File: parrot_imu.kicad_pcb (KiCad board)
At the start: 2 copper layers, 50 x 100 mm, 29 parts, among them J1 Conn_01x02_Male, J2 SI-60062-F, J3 TB005-762-02BE, U1 TR05S3V3, U2 VR10S05, U3 Spark_fun_ICM-20948, U4 Teensy4.1, U5 TJA1441AT/0Z, U6 SOT_24-2BLY_STM

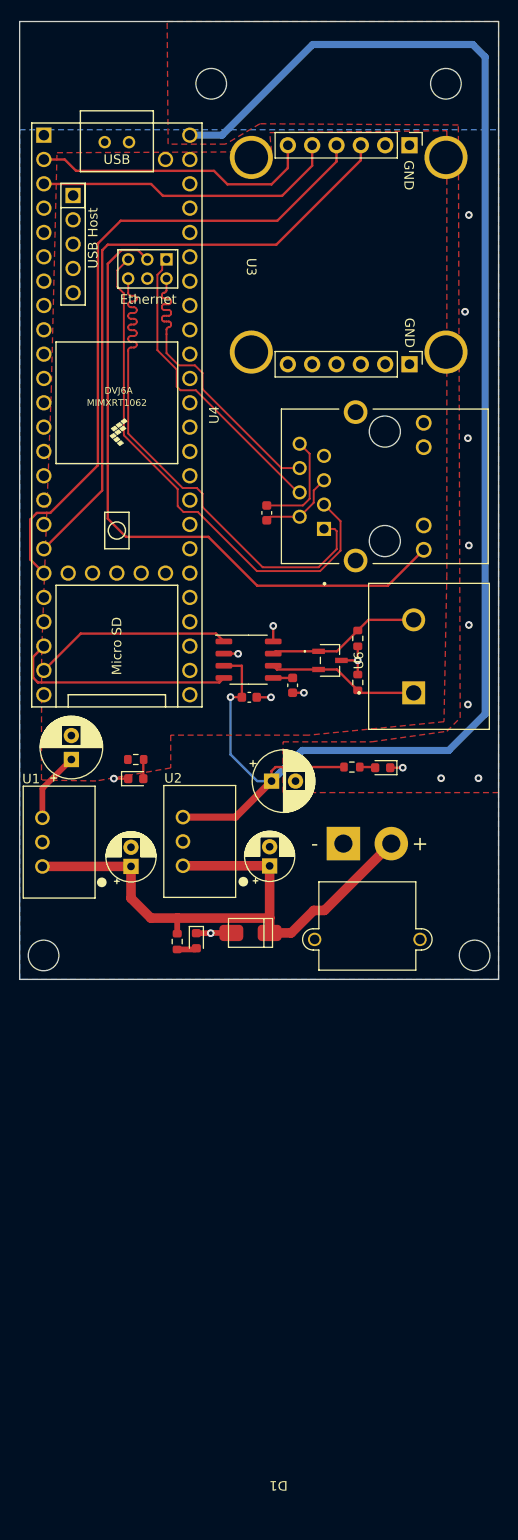
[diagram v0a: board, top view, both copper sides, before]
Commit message: silk screen stuff
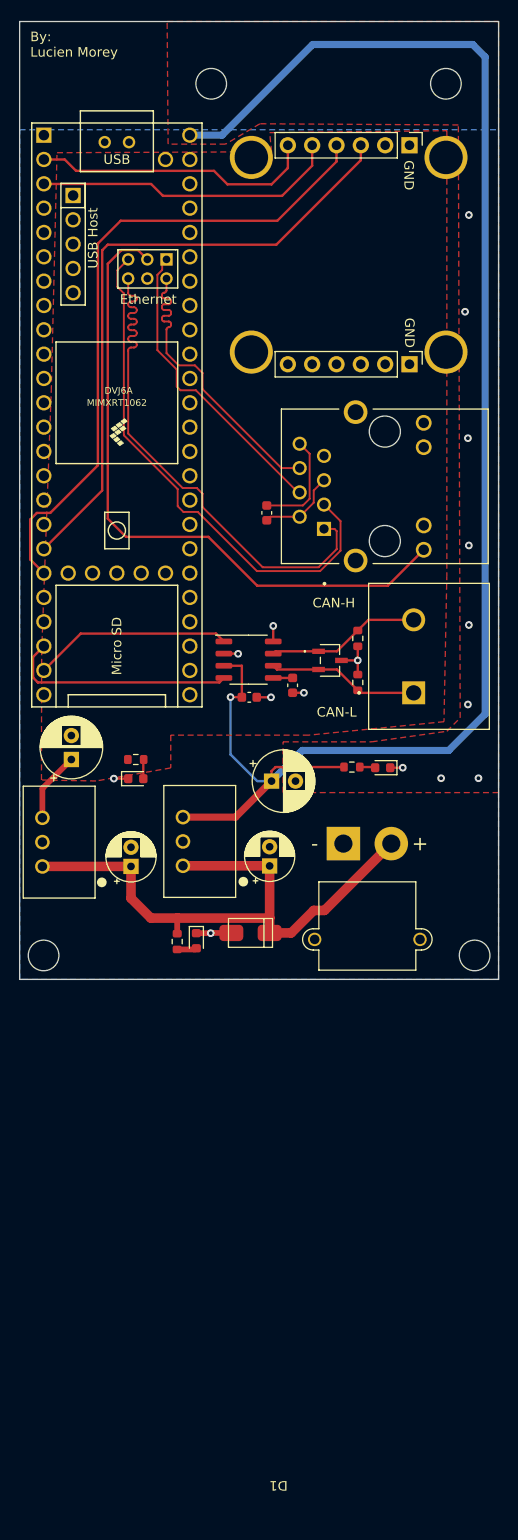
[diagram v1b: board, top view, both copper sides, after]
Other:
- board text added: "By: Lucien Morey"
- board text added: "CAN-H"
- board text added: "CAN-L"
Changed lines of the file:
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@@
     (property "Sheetname" "")
     (attr smd)
-    (fp_text reference "U3" (at -10.16 11.43 -90 unlocked) (layer "F.SilkS")
+    (fp_text reference "U3" (at -10.16 11.43 -90 unlocked) (layer "F.SilkS") hide
       (effects (font (size 1 1) (thickness 0.15)))
     )
@@
     (property "Sheetname" "")
     (attr through_hole)
-    (fp_text reference "U2" (at 6.6 -1.026393 unlocked) (layer "F.SilkS")
+    (fp_text reference "U2" (at 6.6 -1.026393 unlocked) (layer "F.SilkS") hide
       (effects (font (size 1 1) (thickness 0.15)))
     )
@@
     (property "Sheetname" "")
     (attr smd)
-    (fp_text reference "U6" (at 0 -3 -90) (layer "F.SilkS")
+    (fp_text reference "U6" (at 0 -3 -90) (layer "F.SilkS") hide
       (effects (font (size 1 1) (thickness 0.15)))
     )
@@
     (property "Sheetname" "")
     (attr through_hole)
-    (fp_text reference "U4" (at 0 -10.16 90) (layer "F.SilkS")
+    (fp_text reference "U4" (at 0 -10.16 90) (layer "F.SilkS") hide
       (effects (font (size 1 1) (thickness 0.15)))
     )
@@
     (property "Sheetname" "")
     (attr through_hole)
-    (fp_text reference "U1" (at 6.6 -1.176393 unlocked) (layer "F.SilkS")
+    (fp_text reference "U1" (at 6.6 -1.176393 unlocked) (layer "F.SilkS") hide
       (effects (font (size 1 1) (thickness 0.15)))
     )
@@
   (gr_line (start 50 49) (end 100 49) (layer "Edge.Cuts") (width 0.1))
   (gr_line (start 50 149) (end 50 49) (layer "Edge.Cuts") (width 0.1))
+  (gr_text "By:\nLucien Morey" (at 51.1 51.4) (layer "F.SilkS")
+    (effects (font (size 1 1) (thickness 0.15)) (justify left))
+  )
+  (gr_text "CAN-H" (at 82.8 109.7) (layer "F.SilkS")
+    (effects (font (size 1 1) (thickness 0.15)))
+  )
+  (gr_text "CAN-L" (at 83.1 121.1) (layer "F.SilkS")
+    (effects (font (size 1 1) (thickness 0.15)))
+  )
   (segment (start 81.825 141.8) (end 88.8 134.825) (width 1) (layer "F.Cu") (net 1))
   (segment (start 61.625 140.525) (end 63.7 142.6) (width 1) (layer "F.Cu") (net 1))
@@
   (segment (start 79.235 93.08) (end 80.274 94.119) (width 0.2) (layer "F.Cu") (net 2))
   (segment (start 76.475 113.72) (end 76.475 112.1) (width 0.25) (layer "F.Cu") (net 2))
-  (segment (start 79.375 119.075) (end 79.38 119.08) (width 0.25) (layer "F.Cu") (net 2))
   (segment (start 76.24 119.55) (end 74.75 119.55) (width 0.25) (layer "F.Cu") (net 2))
   (segment (start 72.81 115.01) (end 72.79 114.99) (width 0.25) (layer "F.Cu") (net 2))
@@
   (segment (start 76.715625 126.834375) (end 83.8625 126.834375) (width 0.25) (layer "F.Cu") (net 3))
   (segment (start 73.2 119.55) (end 73.2 116.26) (width 0.25) (layer "F.Cu") (net 3))
-  (segment (start 83.8625 126.834375) (end 83.8375 126.859375) (width 0.25) (layer "F.Cu") (net 3))
   (segment (start 72.02 119.53) (end 73.18 119.53) (width 0.25) (layer "F.Cu") (net 3))
   (segment (start 67.051393 132.06) (end 72.54 132.06) (width 0.75) (layer "F.Cu") (net 3))
@@
   (segment (start 62.9125 126.082387) (end 62.95 126.044887) (width 0.25) (layer "F.Cu") (net 6))
   (segment (start 62.9125 128.044887) (end 62.9125 126.082387) (width 0.25) (layer "F.Cu") (net 6))
-  (segment (start 85.5 126.846875) (end 85.5125 126.834375) (width 0.25) (layer "F.Cu") (net 7))
   (segment (start 87.046875 126.834375) (end 87.1125 126.9) (width 0.25) (layer "F.Cu") (net 7))
   (segment (start 85.5125 126.834375) (end 87.046875 126.834375) (width 0.25) (layer "F.Cu") (net 7))
@@
   (segment (start 64.3816 83.3066) (end 66.4 85.325) (width 0.2) (layer "F.Cu") (net 10))
   (segment (start 64.858418 79.954991) (end 64.858418 80.081809) (width 0.2) (layer "F.Cu") (net 11))
-  (segment (start 65.095009 79.1184) (end 65.3316 79.1184) (width 0.2) (layer "F.Cu") (net 11))
+  (segment (start 65.095009 79.1184) (end 65.568191 79.1184) (width 0.2) (layer "F.Cu") (net 11))
   (segment (start 69.1 87.388603) (end 77.331397 95.62) (width 0.2) (layer "F.Cu") (net 11))
-  (segment (start 65.3316 79.7184) (end 65.095009 79.7184) (width 0.2) (layer "F.Cu") (net 11))
-  (segment (start 65.3316 79.1184) (end 65.568191 79.1184) (width 0.2) (layer "F.Cu") (net 11))
+  (segment (start 65.095009 79.7184) (end 65.568191 79.7184) (width 0.2) (layer "F.Cu") (net 11))
   (segment (start 65.3316 77.904991) (end 65.3316 77.9184) (width 0.2) (layer "F.Cu") (net 11))
   (segment (start 68.3 84.9) (end 69.1 85.7) (width 0.2) (layer "F.Cu") (net 11))
   (segment (start 65.3316 83.620203) (end 66.611397 84.9) (width 0.2) (layer "F.Cu") (net 11))
-  (segment (start 65.568191 78.5184) (end 65.3316 78.5184) (width 0.2) (layer "F.Cu") (net 11))
+  (segment (start 65.095009 78.5184) (end 65.568191 78.5184) (width 0.2) (layer "F.Cu") (net 11))
   (segment (start 65.3316 75.835) (end 65.3316 77.0684) (width 0.2) (layer "F.Cu") (net 11))
-  (segment (start 65.3316 78.5184) (end 65.095009 78.5184) (width 0.2) (layer "F.Cu") (net 11))
   (segment (start 64.858418 77.541582) (end 64.858418 77.6684) (width 0.2) (layer "F.Cu") (net 11))
   (segment (start 77.331397 95.62) (end 79.235 95.62) (width 0.2) (layer "F.Cu") (net 11))
@@
   (segment (start 66.611397 84.9) (end 68.3 84.9) (width 0.2) (layer "F.Cu") (net 11))
   (segment (start 65.804782 78.154991) (end 65.804782 78.281809) (width 0.2) (layer "F.Cu") (net 11))
-  (segment (start 65.568191 79.7184) (end 65.3316 79.7184) (width 0.2) (layer "F.Cu") (net 11))
   (segment (start 65.804782 79.354991) (end 65.804782 79.481809) (width 0.2) (layer "F.Cu") (net 11))
-  (segment (start 65.3316 80.3184) (end 65.568191 80.3184) (width 0.2) (layer "F.Cu") (net 11))
+  (segment (start 65.095009 80.3184) (end 65.568191 80.3184) (width 0.2) (layer "F.Cu") (net 11))
   (segment (start 69.1 85.7) (end 69.1 87.388603) (width 0.2) (layer "F.Cu") (net 11))
   (segment (start 65.804782 80.554991) (end 65.804782 80.681809) (width 0.2) (layer "F.Cu") (net 11))
-  (segment (start 65.095009 80.3184) (end 65.3316 80.3184) (width 0.2) (layer "F.Cu") (net 11))
-  (segment (start 65.3316 81.637442) (end 65.3316 83.620203) (width 0.2) (layer "F.Cu") (net 11))
-  (segment (start 65.3316 81.154991) (end 65.3316 81.637442) (width 0.2) (layer "F.Cu") (net 11))
+  (segment (start 65.3316 81.154991) (end 65.3316 83.620203) (width 0.2) (layer "F.Cu") (net 11))
   (segment (start 64.858418 78.754991) (end 64.858418 78.881809) (width 0.2) (layer "F.Cu") (net 11))
   (arc (start 64.858418 80.081809) (mid 64.927714 80.249104) (end 65.095009 80.3184) (width 0.2) (layer "F.Cu") (net 11))

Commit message: add tony fixes from design review
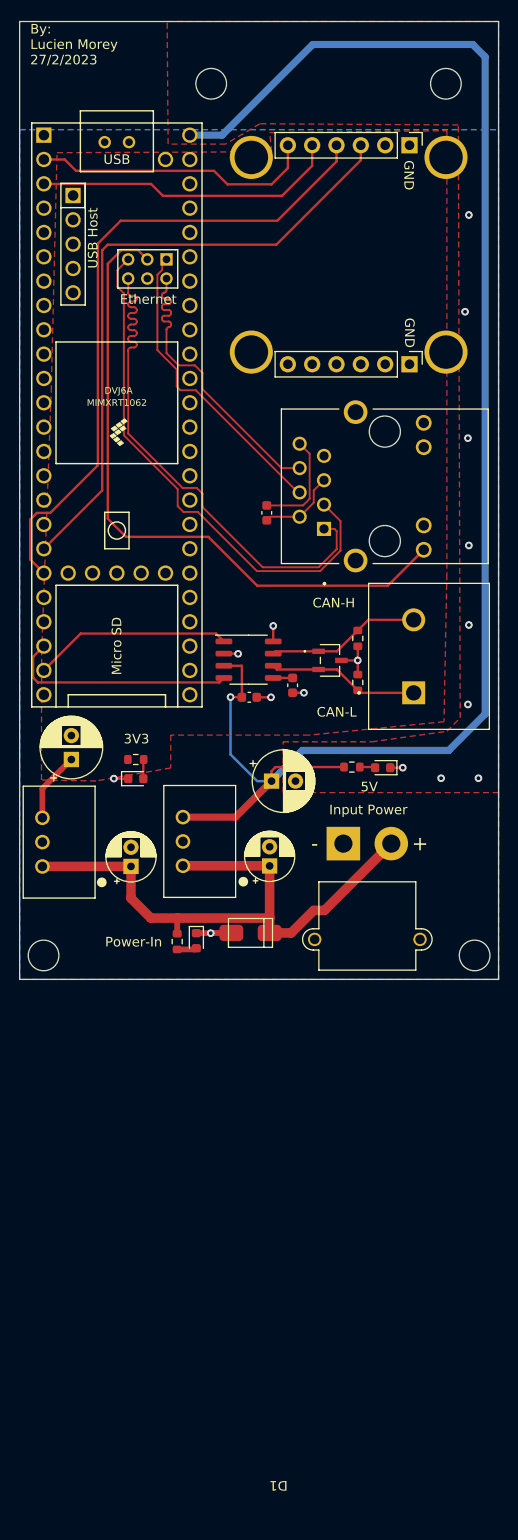
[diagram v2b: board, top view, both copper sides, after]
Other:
- board text added: "3V3"
- board text added: "5V"
- board text added: "By: Lucien Morey 27/2/2023"
- board text added: "Input Power"
- board text added: "Power-In"
- board text removed: "By: Lucien Morey"
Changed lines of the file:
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@@
   (gr_line (start 50 49) (end 100 49) (layer "Edge.Cuts") (width 0.1))
   (gr_line (start 50 149) (end 50 49) (layer "Edge.Cuts") (width 0.1))
-  (gr_text "By:\nLucien Morey" (at 51.1 51.4) (layer "F.SilkS")
+  (gr_text "Power-In" (at 61.9 145.1) (layer "F.SilkS")
+    (effects (font (size 1 1) (thickness 0.15)))
+  )
+  (gr_text "By:\nLucien Morey\n27/2/2023" (at 51.1 51.4) (layer "F.SilkS")
     (effects (font (size 1 1) (thickness 0.15)) (justify left))
   )
@@
     (effects (font (size 1 1) (thickness 0.15)))
   )
+  (gr_text "5V\n" (at 86.5 128.9) (layer "F.SilkS")
+    (effects (font (size 1 1) (thickness 0.15)))
+  )
+  (gr_text "Input Power" (at 86.4 131.3) (layer "F.SilkS")
+    (effects (font (size 1 1) (thickness 0.15)))
+  )
+  (gr_text "3V3" (at 62.2 123.9) (layer "F.SilkS")
+    (effects (font (size 1 1) (thickness 0.15)))
+  )

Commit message: update pcb
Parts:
- U6: value SOT_24-2BLY_STM -> ESDCAN24-2BLY
- moved H4 24.5 mm to (94.5, 55.5)
- moved H2 23.6 mm to (70.9, 55.5)
- moved C1 7.73 mm to (60.9, 144.9), turned to -90 degrees
- moved U4 7.16 mm to (60.0, 97.2)
- moved C4 6.84 mm to (54.4, 132.8)
- moved U1 5.49 mm to (57.3, 137.1), turned to 0 degrees
- moved D3 4.89 mm to (61.0, 132.8)
- moved R2 4.89 mm to (61.0, 130.8)
- moved U2 2.97 mm to (70.0, 134.7), turned to -90 degrees
- moved D1 2.87 mm to (73.0, 146.8)
- moved D2 2.06 mm to (70.4, 144.3), turned to 180 degrees
- moved H1 1.50 mm to (96.0, 146.5)
- moved R1 1.45 mm to (67.9, 145.1), turned to 90 degrees
- moved J1 1.20 mm to (82.6, 134.8)
- moved C2 1.10 mm to (75.0, 137.2)
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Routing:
- net /MOSI: track 66.1 -> 81.5 mm
- net /Eth_tx-: track 55.1 -> 42.1 mm
- net /Eth_tx+: track 54.8 -> 42.0 mm
- net +5V: track 166.5 -> 174.7 mm
- net /Eth_led: track 69.2 -> 61.8 mm
- net Net-(C1-Pad1): track 62.2 -> 66.7 mm
- net /Eth_rx+: track 31.9 -> 27.5 mm
- net /Eth_rx-: track 31.8 -> 27.4 mm
- net /Can_rx: track 24.1 -> 27.0 mm
- net +3.3V: track 9.36 -> 6.58 mm
- net /MISO: track 32.0 -> 34.7 mm
- net /Can_tx: track 20.7 -> 23.2 mm
- net /SCK: track 68.9 -> 71.3 mm
- net /CS: track 29.6 -> 30.7 mm
- net GND: track 27.8 -> 27.2 mm, vias 16 -> 17
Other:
- board text added: "By: Lucien Morey v1.3 13/3/2023"
- board text removed: "By: Lucien Morey 27/2/2023"
